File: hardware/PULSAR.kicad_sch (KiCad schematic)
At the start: 4 parts, among them U1 AP2112K-3.3, U2 SS49E

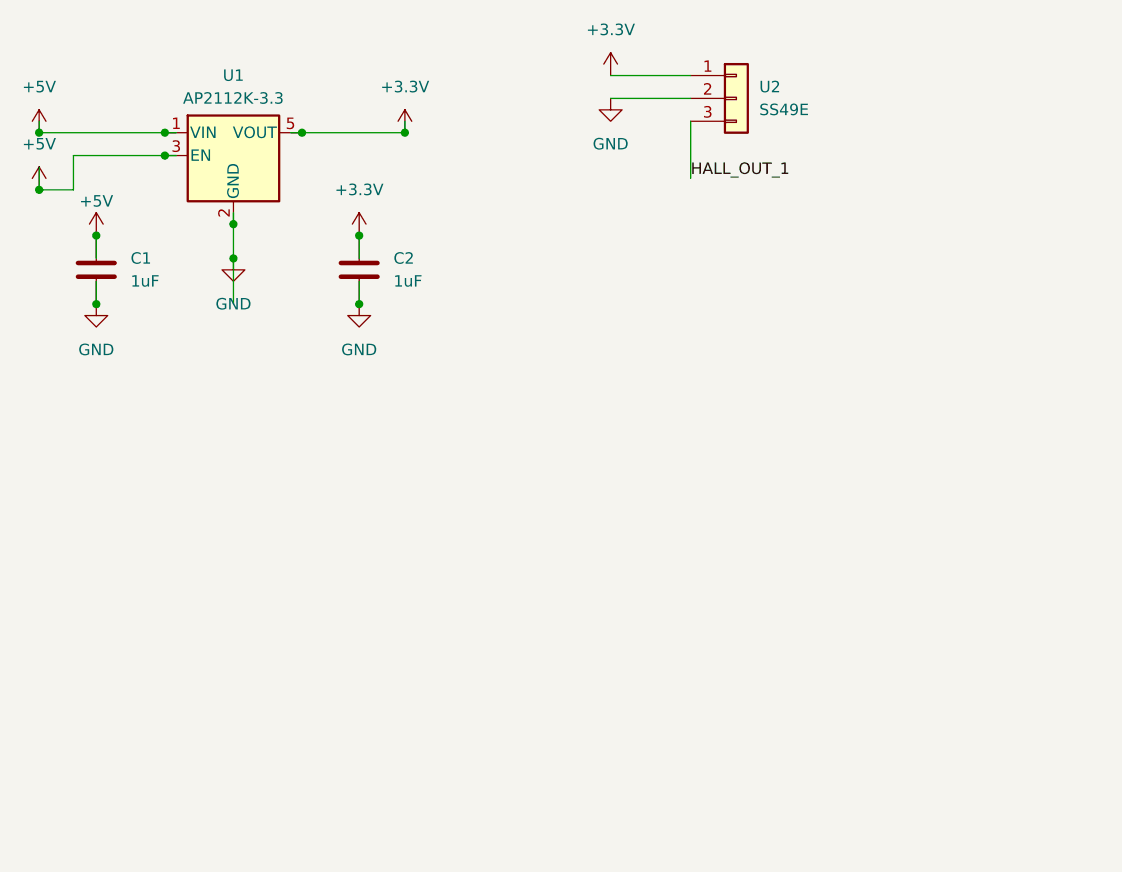
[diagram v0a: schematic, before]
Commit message: feat: add MUX CD74HC4067M schematic with control signals
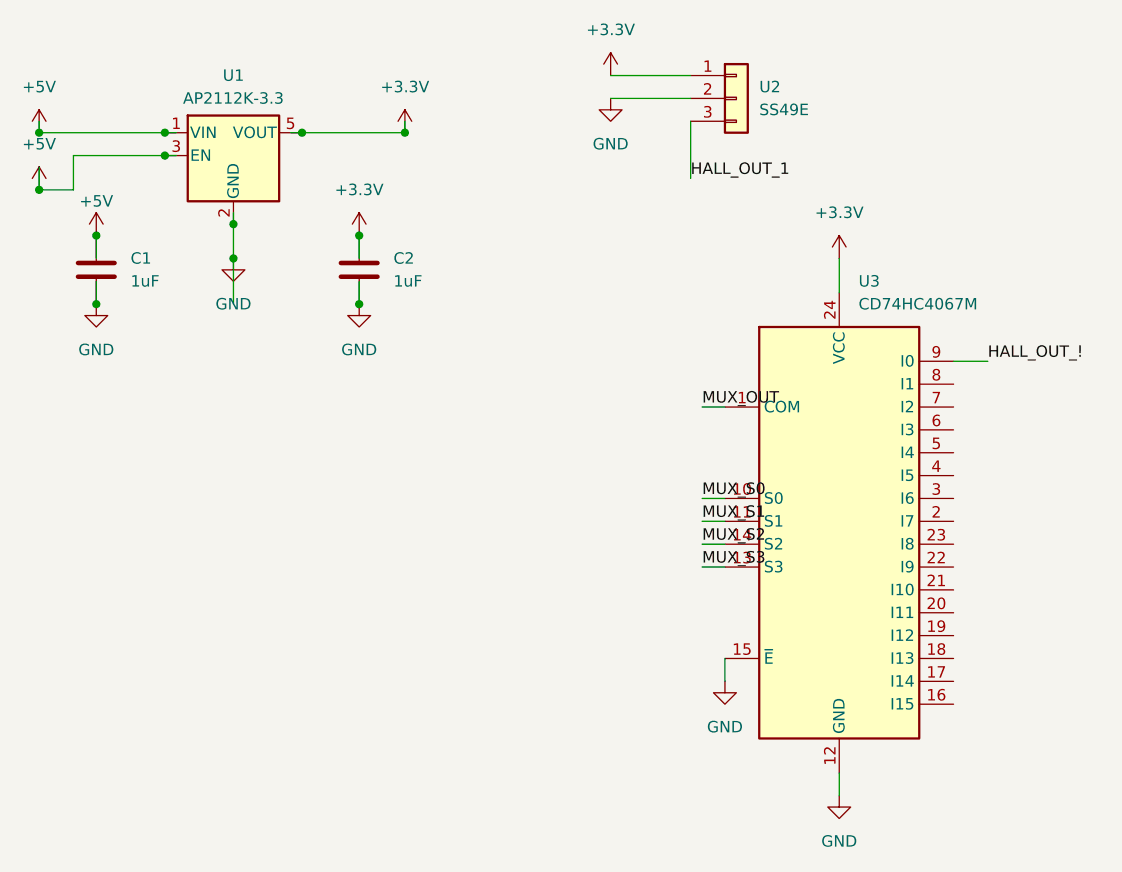
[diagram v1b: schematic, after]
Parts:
- added U3: CD74HC4067M, Package_SO:SOIC-24W_7.5x15.4mm_P1.27mm, symbol 74xx:CD74HC4067M
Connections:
- net +3.3V: now also U3.24 (VCC)
- net GND: now also U3.12 (GND), U3.15 (~{E})
- new net HALL_OUT_!: U3.9 (I0)
- new net MUX_OUT: U3.1 (COM)
- new net MUX_S0: U3.10 (S0)
- new net MUX_S1: U3.11 (S1)
- new net MUX_S2: U3.14 (S2)
- new net MUX_S3: U3.13 (S3)
